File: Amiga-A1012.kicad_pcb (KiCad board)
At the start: 2 copper layers, 90.2 x 82.9 mm, 20 parts, among them U1 74LS38, U2 74LS74, U3 74LS38

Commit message: Added Front/Back texts, added copyright/date.
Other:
- board text added: "A1012 (C) Sören Gust 2017-04-30"
- board text added: "Back"
- board text added: "Front"
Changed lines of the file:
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@@
     (area 129.111904 67.507 234.973 156.57)
     (thickness 1.6)
-    (drawings 8)
+    (drawings 11)
     (tracks 399)
     (zones 0)
@@
     (pad 1 np_thru_hole circle (at 0 0) (size 4 4) (drill 4) (layers *.Cu *.Mask))
   )
+  (gr_text "A1012 (C) Sören Gust 2017-04-30" (at 185.928 76.581) (layer F.Cu)
+    (effects (font (size 1.5 1.5) (thickness 0.3)))
+  )
+  (gr_text Back (at 162.179 76.581) (layer B.Cu)
+    (effects (font (size 1.5 1.5) (thickness 0.3)) (justify mirror))
+  )
+  (gr_text Front (at 155.702 76.581) (layer F.Cu)
+    (effects (font (size 1.5 1.5) (thickness 0.3)))
+  )
   (dimension 90.17 (width 0.3) (layer F.Fab)

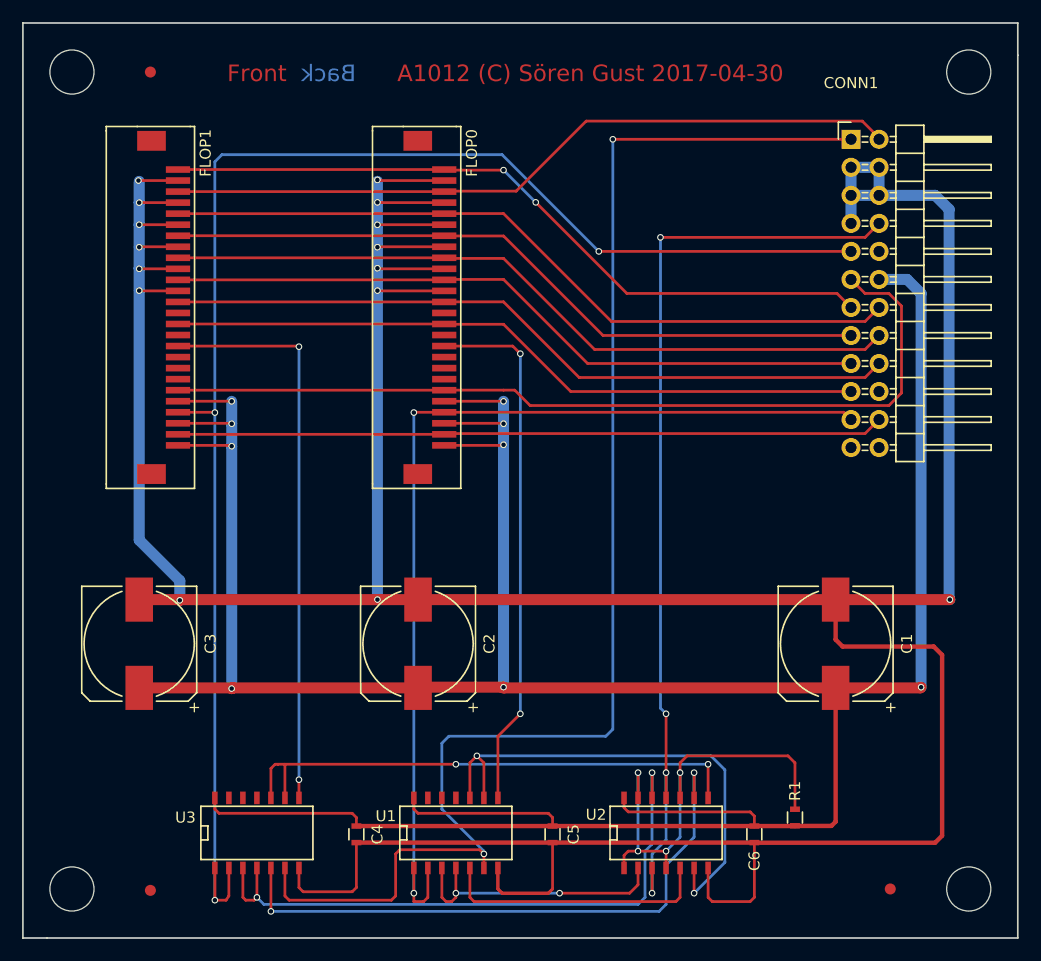
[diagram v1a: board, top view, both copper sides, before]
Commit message: Work in progress, fixing problems found in prototype:  * swapped clock and data on LS74  * need pull-up on LS38 to LS74  * add pull-ups on unused LS38 gates  * connect drive reset
Started to reduce size.
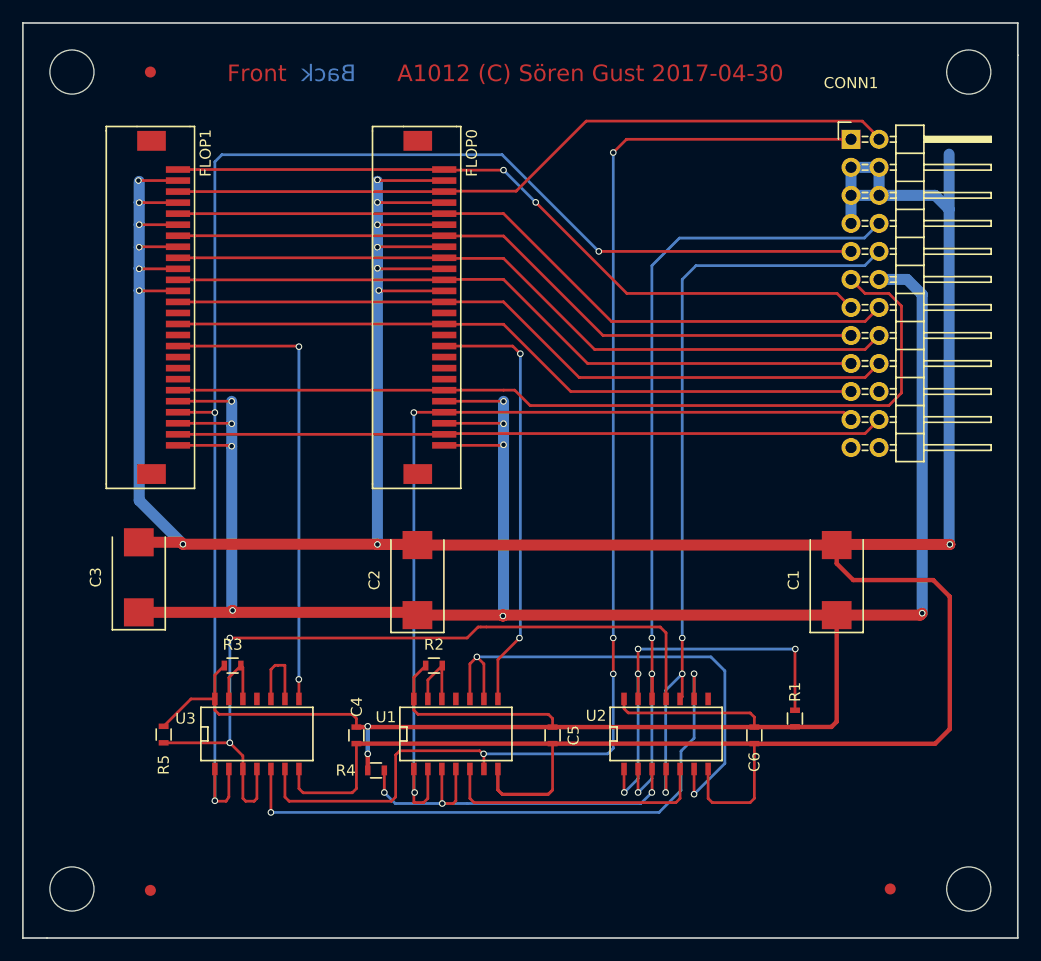
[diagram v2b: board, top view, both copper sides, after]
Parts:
- added R2: 1K, Resistors_SMD:R_0603, F.Cu at (171.8, 130.2)
- added R3: 1K, Resistors_SMD:R_0603, F.Cu at (153.5, 130.2)
- added R4: 1K, Resistors_SMD:R_0603, F.Cu at (166.5, 139.8)
- added R5: 1K, Resistors_SMD:R_0603, F.Cu at (147.2, 136.5)
- C1, C2, C3: value 1000µF -> 470µF/10V; footprint Capacitors_SMD:c_elec_10x10.5 -> Capacitors_Tantalum_SMD:Tantalum_Case-D_EIA-7343-31_Reflow
- R1: value 4K7 -> 1K
- moved C4 8.97 mm to (164.7, 136.6)
- moved C5 8.97 mm to (182.5, 136.6)
- moved C6 8.97 mm to (200.8, 136.6)
- moved R1 8.97 mm to (204.5, 135.0)
- moved U1 8.97 mm to (173.7, 136.3)
- moved U2 8.97 mm to (192.8, 136.3)
- moved U3 8.97 mm to (155.7, 136.3)
- moved C3 6.02 mm to (145.0, 122.2)
- moved C1 5.77 mm to (208.2, 122.5)
- moved C2 5.77 mm to (170.2, 122.5)
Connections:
- U1 pad 11: (no net) -> Net-(U1-Pad11)
- U1 pad 12: (no net) -> Net-(R2-Pad2)
- U1 pad 13: (no net) -> Net-(R2-Pad2)
- U1 pad 3: Net-(U1-Pad3) -> Net-(R4-Pad2)
- U1 pad 4: Net-(U1-Pad3) -> Net-(R4-Pad2)
- U2 pad 10: Net-(R1-Pad2) -> Net-(CONN1-Pad10)
- U2 pad 11: Net-(CONN1-Pad8) -> Net-(R5-Pad2)
- U2 pad 12: Net-(U2-Pad12) -> Net-(CONN1-Pad8)
- U2 pad 2: Net-(U1-Pad3) -> Net-(CONN1-Pad8)
- U2 pad 3: Net-(CONN1-Pad8) -> Net-(R4-Pad2)
- U2 pad 4: Net-(R1-Pad2) -> Net-(CONN1-Pad10)
- U3 pad 11: (no net) -> Net-(U3-Pad11)
- U3 pad 12: (no net) -> Net-(R3-Pad2)
- U3 pad 13: (no net) -> Net-(R3-Pad2)
- U3 pad 3: Net-(U2-Pad12) -> Net-(R5-Pad2)
- U3 pad 4: Net-(U2-Pad12) -> Net-(R5-Pad2)
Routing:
- net Net-(R5-Pad2): track 0.00 -> 71.3 mm, vias 0 -> 2
- net Net-(CONN1-Pad10): track 0.00 -> 70.7 mm, vias 0 -> 3
- net Net-(U2-Pad12): track 56.4 -> 0.00 mm, vias 2 -> 0
- net Net-(U2-Pad8): track 48.5 -> 7.14 mm, vias 2 -> 0
- net Net-(R4-Pad2): track 0.00 -> 36.6 mm, vias 0 -> 3
- net Net-(U1-Pad3): track 25.3 -> 0.00 mm, vias 2 -> 0
- net Net-(CONN1-Pad1): track 129.0 -> 114.4 mm, vias 2 -> 4
- net Net-(CONN1-Pad9): track 138.8 -> 129.8 mm
- net Net-(FLOP1-Pad10): track 51.9 -> 42.9 mm
- net Net-(CONN1-Pad21): track 90.6 -> 81.7 mm
- net Net-(FLOP0-Pad10): track 48.3 -> 39.4 mm
- net Net-(CONN1-Pad8): track 85.1 -> 77.1 mm, vias 4 -> 3
- net Net-(R2-Pad2): track 0.00 -> 6.59 mm
- net Net-(R3-Pad2): track 0.00 -> 6.57 mm
- net GND: track 389.2 -> 383.3 mm
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
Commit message: Finished routing, board is much smaller now.
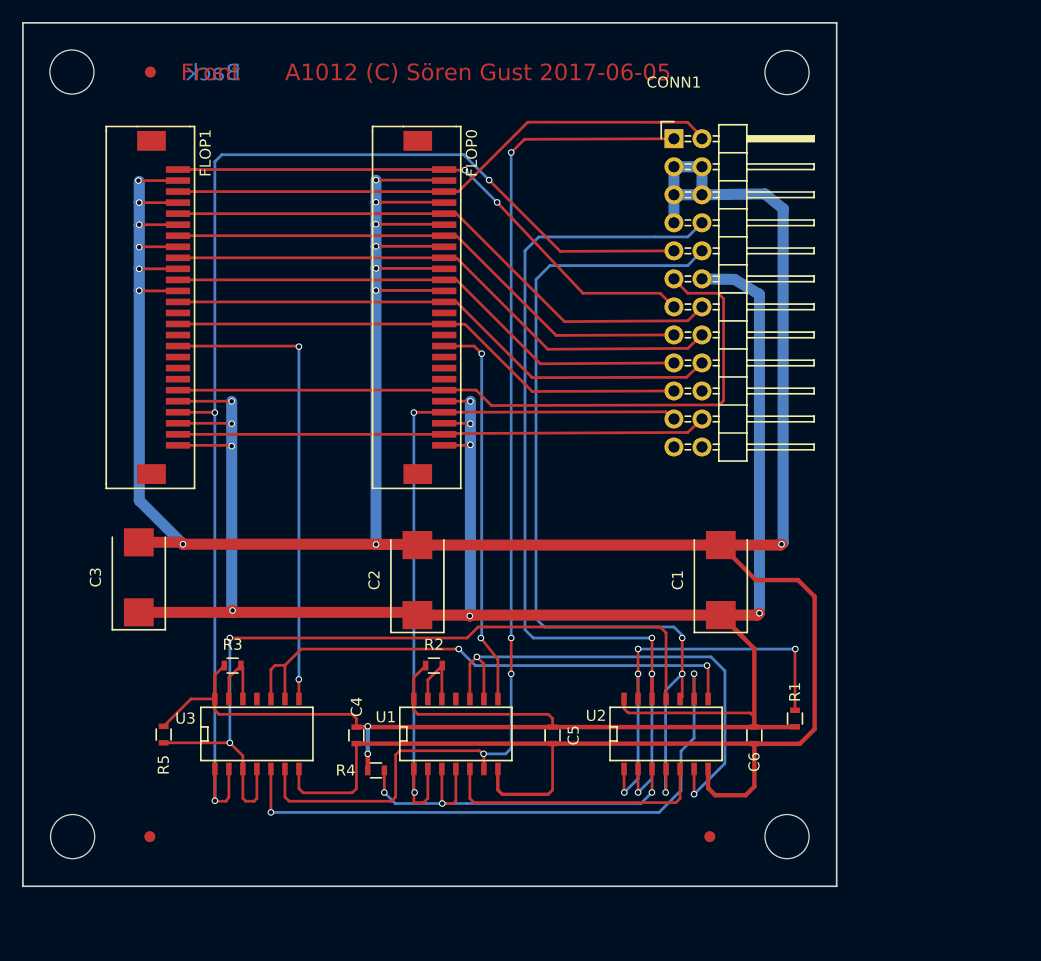
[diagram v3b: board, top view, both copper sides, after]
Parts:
- moved REF** 17.1 mm to (203.8, 145.8)
- moved REF** 17.0 mm to (196.8, 145.8)
- moved REF** 16.5 mm to (203.8, 76.5)
- moved CONN1 16.1 mm to (193.5, 82.5)
- moved C1 10.5 mm to (197.8, 122.5)
- moved REF** 4.87 mm to (146.0, 145.8)
- moved REF** 4.75 mm to (139.0, 145.8)
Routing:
- net Net-(U2-Pad8): track 7.14 -> 49.7 mm, vias 0 -> 2
- net GND: track 383.3 -> 345.1 mm
- net +5V: track 288.3 -> 266.4 mm
- net Net-(CONN1-Pad2): track 66.9 -> 50.8 mm
- net Net-(CONN1-Pad22): track 64.1 -> 48.0 mm
- net Net-(CONN1-Pad16): track 67.5 -> 51.4 mm
- net Net-(CONN1-Pad21): track 81.7 -> 65.7 mm
- net Net-(CONN1-Pad18): track 66.9 -> 50.8 mm
- net Net-(CONN1-Pad14): track 68.1 -> 52.1 mm
- net Net-(CONN1-Pad19): track 63.5 -> 47.5 mm
- net Net-(CONN1-Pad15): track 64.7 -> 48.7 mm
- net Net-(CONN1-Pad17): track 64.2 -> 48.1 mm
- net Net-(CONN1-Pad1): track 114.4 -> 98.4 mm
- net Net-(CONN1-Pad9): track 129.8 -> 113.8 mm
- net Net-(CONN1-Pad13): track 66.2 -> 50.2 mm
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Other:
- board size 90.2 x 82.9 mm -> 73.8 x 78.2 mm
- board text added: "A1012 (C) Sören Gust 2017-06-05"
- board text removed: "A1012 (C) Sören Gust 2017-04-30"

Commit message: Made all vias bigger to allow cheaper eurocircuits manufacturing.
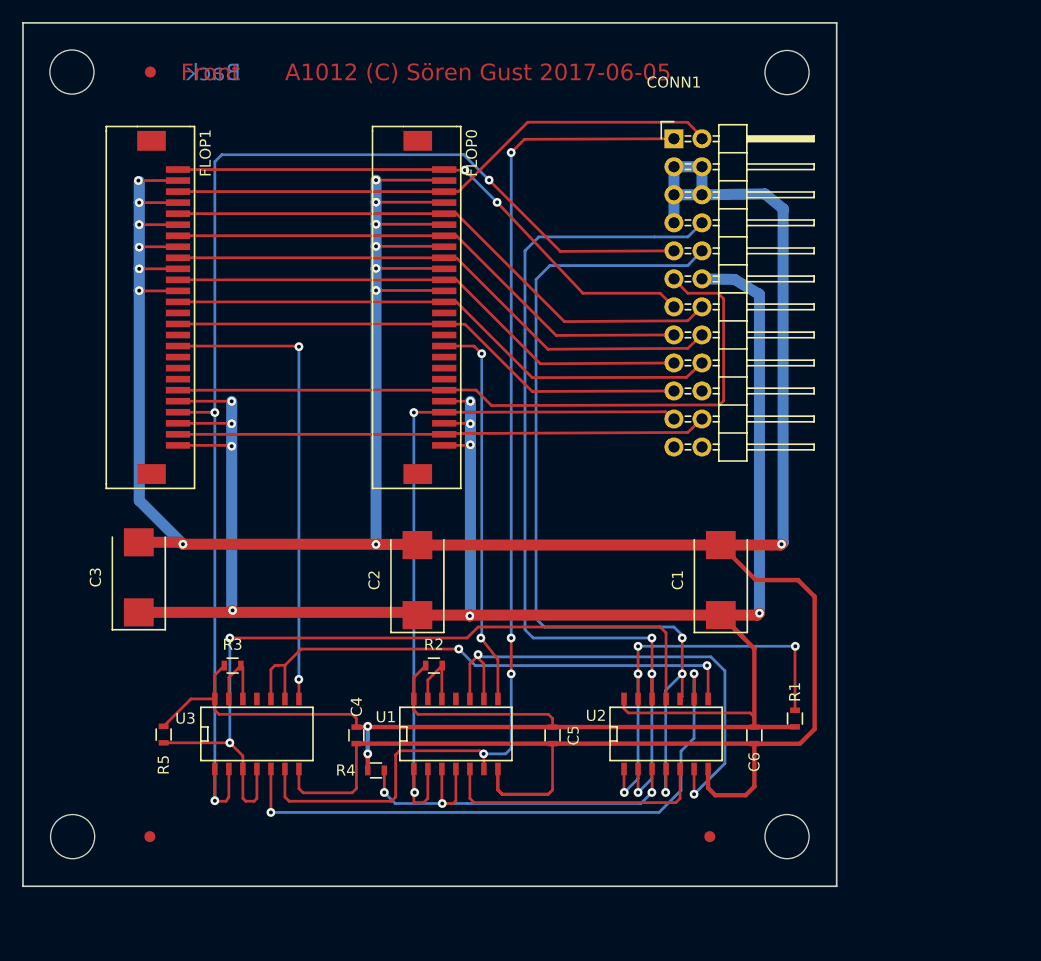
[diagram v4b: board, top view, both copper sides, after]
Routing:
- net Net-(R1-Pad2): track 37.7 -> 38.2 mm
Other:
- net class Default: via_dia 0.6 -> 0.8; via_drill 0.4 -> 0.35
- rule via_min_drill: 0.3 -> 0.35
- rule via_min_size: 0.4 -> 0.8

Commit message: Named holes and fiducials.
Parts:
- renumbered REF** to Hole1, REF** to Hole2, REF** to Hole3, REF** to Hole4, REF** to Marker1, REF** to Marker2, REF** to Marker3
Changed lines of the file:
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@@
     (tags marker)
     (attr virtual)
-    (fp_text reference REF** (at 4.064 0) (layer F.SilkS) hide
+    (fp_text reference Marker2 (at 4.064 0) (layer F.SilkS) hide
       (effects (font (size 1 1) (thickness 0.15)))
     )
@@
     (tags marker)
     (attr virtual)
-    (fp_text reference REF** (at 3.4 0.7) (layer F.SilkS) hide
+    (fp_text reference Marker1 (at 3.4 0.7) (layer F.SilkS) hide
       (effects (font (size 1 1) (thickness 0.15)))
     )
@@
     (tags marker)
     (attr virtual)
-    (fp_text reference REF** (at -4.064 0) (layer F.SilkS) hide
+    (fp_text reference Marker3 (at -4.064 0) (layer F.SilkS) hide
       (effects (font (size 1 1) (thickness 0.15)))
     )
@@
     (descr "Mounting Hole 4mm, no annular")
     (tags "mounting hole 4mm no annular")
-    (fp_text reference REF** (at 0 -5) (layer F.SilkS) hide
+    (fp_text reference Hole1 (at 0 -5) (layer F.SilkS) hide
       (effects (font (size 1 1) (thickness 0.15)))
     )
@@
     (descr "Mounting Hole 4mm, no annular")
     (tags "mounting hole 4mm no annular")
-    (fp_text reference REF** (at 0 -5) (layer F.SilkS) hide
+    (fp_text reference Hole3 (at 0 -5) (layer F.SilkS) hide
       (effects (font (size 1 1) (thickness 0.15)))
     )
@@
     (descr "Mounting Hole 4mm, no annular")
     (tags "mounting hole 4mm no annular")
-    (fp_text reference REF** (at 0 -5) (layer F.SilkS) hide
+    (fp_text reference Hole4 (at 0 -5) (layer F.SilkS) hide
       (effects (font (size 1 1) (thickness 0.15)))
     )
@@
     (descr "Mounting Hole 4mm, no annular")
     (tags "mounting hole 4mm no annular")
-    (fp_text reference REF** (at 0 -5) (layer F.SilkS) hide
+    (fp_text reference Hole2 (at 0 -5) (layer F.SilkS) hide
       (effects (font (size 1 1) (thickness 0.15)))
     )
